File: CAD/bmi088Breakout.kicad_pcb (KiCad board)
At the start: 2 copper layers, 12.7 x 12.7 mm, 8 parts, among them J1 Conn_01x04_Male, U1 BMI088

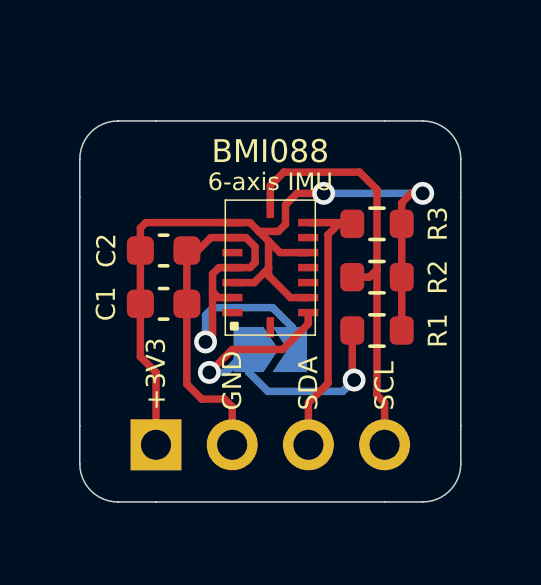
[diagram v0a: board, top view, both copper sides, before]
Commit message: added castellated holes to board
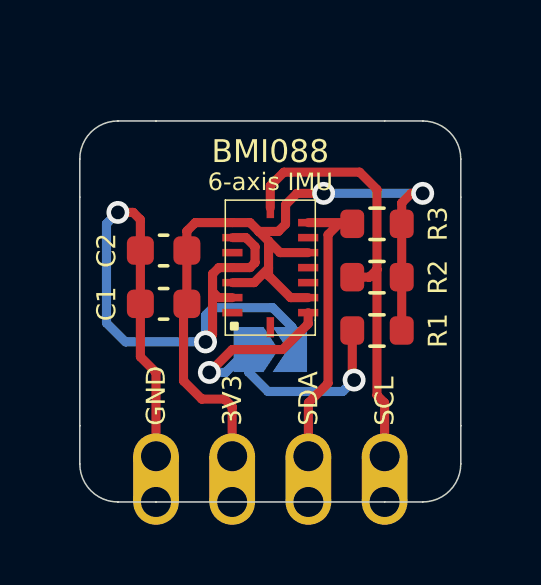
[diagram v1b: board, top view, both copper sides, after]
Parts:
- J1: value Conn_01x04_Male -> Castellated_Conn_01x04; footprint Connector_PinHeader_2.54mm:PinHeader_1x04_P2.54mm_Vertical -> DS-connectors:Castellated_PinHeader_01x04_P2.54mm_Vertical
- moved J1 2.57 mm to (138.4, 84.8)
- turned C1 to 180 degrees
- turned C2 to 180 degrees
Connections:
- J1 pad 1: +3V3 -> GND
- J1 pad 2: GND -> +3V3
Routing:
- net GND: track 20.3 -> 27.3 mm, vias 1 -> 2
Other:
- board text added: "3V3"
- board text removed: "+3V3"

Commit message: Add files via upload
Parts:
- added J2: Castellated_Conn_01x01, DS-connectors:Castellated_PinHeader_01x01_P2.54mm_Vertical, F.Cu at (138.9, 73.9)
- added J3: Castellated_Conn_01x01, DS-connectors:Castellated_PinHeader_01x01_P2.54mm_Vertical, F.Cu at (146.6, 73.9)
- C1, C2: footprint Capacitor_SMD:C_0603_1608Metric -> Capacitor_SMD:C_0805_2012Metric
- R1, R2, R3: footprint Resistor_SMD:R_0603_1608Metric -> Resistor_SMD:R_0805_2012Metric
- moved C1 0.36 mm to (141.0, 80.0)
- moved R1 0.36 mm to (148.6, 80.9)
- moved R3 0.36 mm to (148.6, 76.8)
- moved C2 0.36 mm to (141.0, 77.7)
- moved R2 0.25 mm to (148.6, 78.9)
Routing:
- net GND: track 27.3 -> 42.3 mm
- net SDA: track 10.1 -> 19.4 mm, vias 0 -> 1
- net +3V3: track 28.9 -> 34.5 mm, vias 2 -> 5
- net SCL: track 14.7 -> 15.5 mm
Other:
- board size 12.7 x 12.7 mm -> 14 x 14 mm
